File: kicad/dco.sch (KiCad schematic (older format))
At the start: 19 parts

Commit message: Add simple voltage control
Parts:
- added C?: 100n, symbol Device:C
- added D? (x2): 1N4148, Diode_THT:D_DO-35_SOD27_P7.62mm_Horizontal, symbol Diode:1N4148
- added R?: 10k, symbol Device:R
- A?: value Arduino_Nano_v2.x -> Arduino Nano 328p 16Mhz; symbol MCU_Module:Arduino_Nano_v2.x -> MCU_Module:Arduino_Nano_v3.x
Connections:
- net +5V: now also D?.1 (K)
- net GND: now also C?.2, D?.2 (A)
- net CV: now reaches A?.19 (A0)
- net CV: now also C?.1, D?.1 (K), D?.2 (A), R?.1
- new net CV_IN: R?.2
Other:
- moved on the sheet: C?, Q?, R?, U?, U?A, U?B, U?C

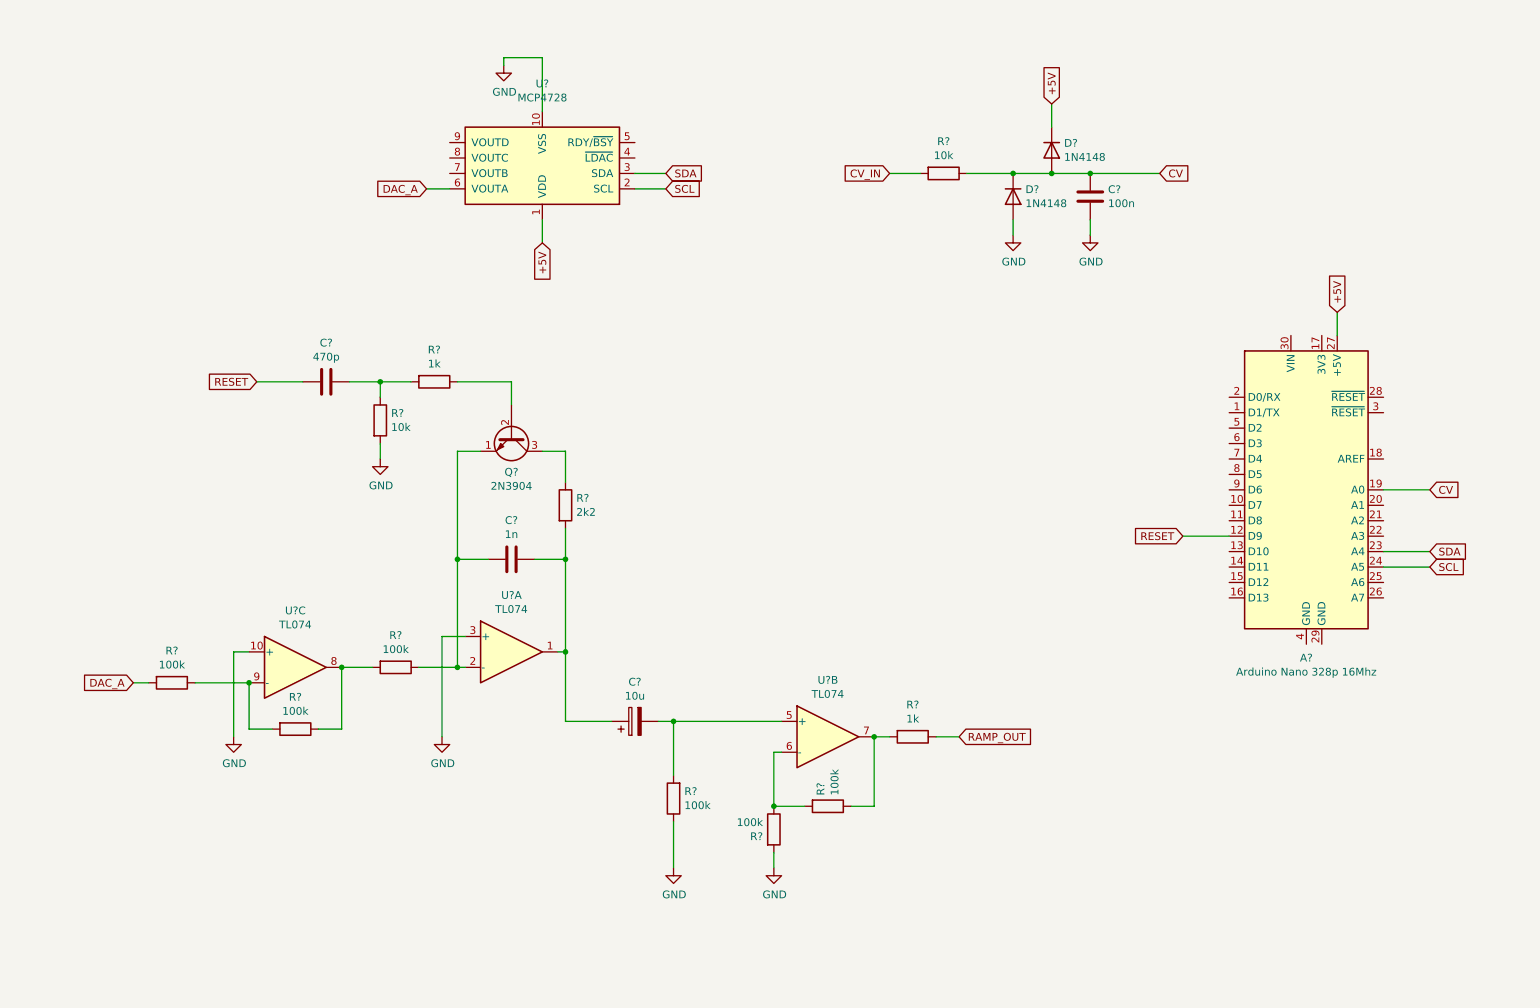
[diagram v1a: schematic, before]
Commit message: Added proper voltage control and pulse out
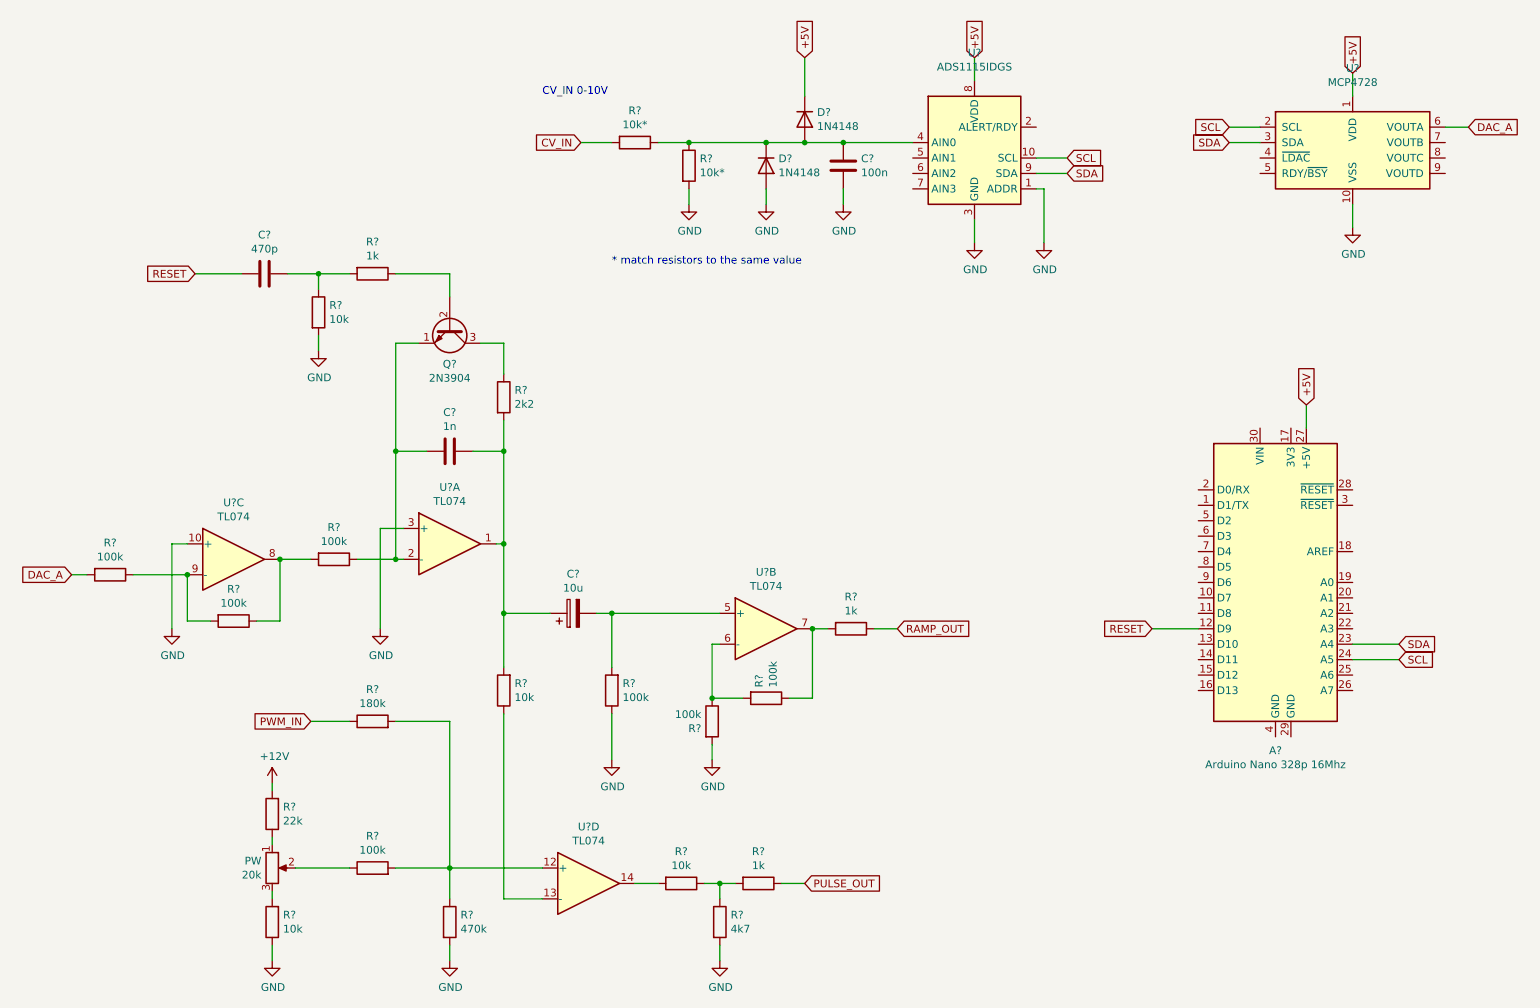
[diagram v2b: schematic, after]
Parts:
- added PW: 20k, symbol Device:R_POT
- added R?: 10k*, symbol Device:R
- added R? (x3): 10k, symbol Device:R
- added R?: 1k, symbol Device:R
- added R?: 470k, symbol Device:R
- added R?: 180k, symbol Device:R
- added R?: 100k, symbol Device:R
- added R?: 22k, symbol Device:R
- added R?: 4k7, symbol Device:R
- added U?: ADS1115IDGS, Package_SO:TSSOP-10_3x3mm_P0.5mm, symbol Analog_ADC:ADS1115IDGS
- added U?: TL074, symbol Amplifier_Operational:TL074
- R?: value 10k -> 10k*
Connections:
- net +5V: now also U?.8 (VDD)
- net GND: now also R?.1, R?.2, R?.2, R?.2, U?.1 (ADDR), U?.3 (GND)
- net SCL: now also U?.10 (SCL)
- net SDA: now also U?.9 (SDA)
- net at C?.1, C?.1, R?.2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: now also R?.2
- net CV: no longer names the net of C?.1, D?.1 (K), D?.2 (A), R?.1
- net CV: now also R?.1, U?.4 (AIN0); no longer A?.19 (A0)
- new net: R?.1, R?.2, R?.2, U?.12 (+)
- new net: R?.1, U?.13 (-)
- new net: R?.2, U?.14
- new net: R?.1, R?.1, R?.2
- new net: PW.2, R?.1
- new net: PW.3, R?.2
- new net: PW.1, R?.1
- new net +12V: R?.2
- new net PULSE_OUT: R?.1
- new net PWM_IN: R?.1
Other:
- note added: "* match resistors to the same value\n"
- note added: "CV_IN 0-10V"
- moved on the sheet: A?, C?, D?, Q?, R?, U?, U?A, U?B, U?C
